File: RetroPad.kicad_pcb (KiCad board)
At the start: 2 copper layers, 125 x 45 mm, 16 parts, among them J1 5747840-3

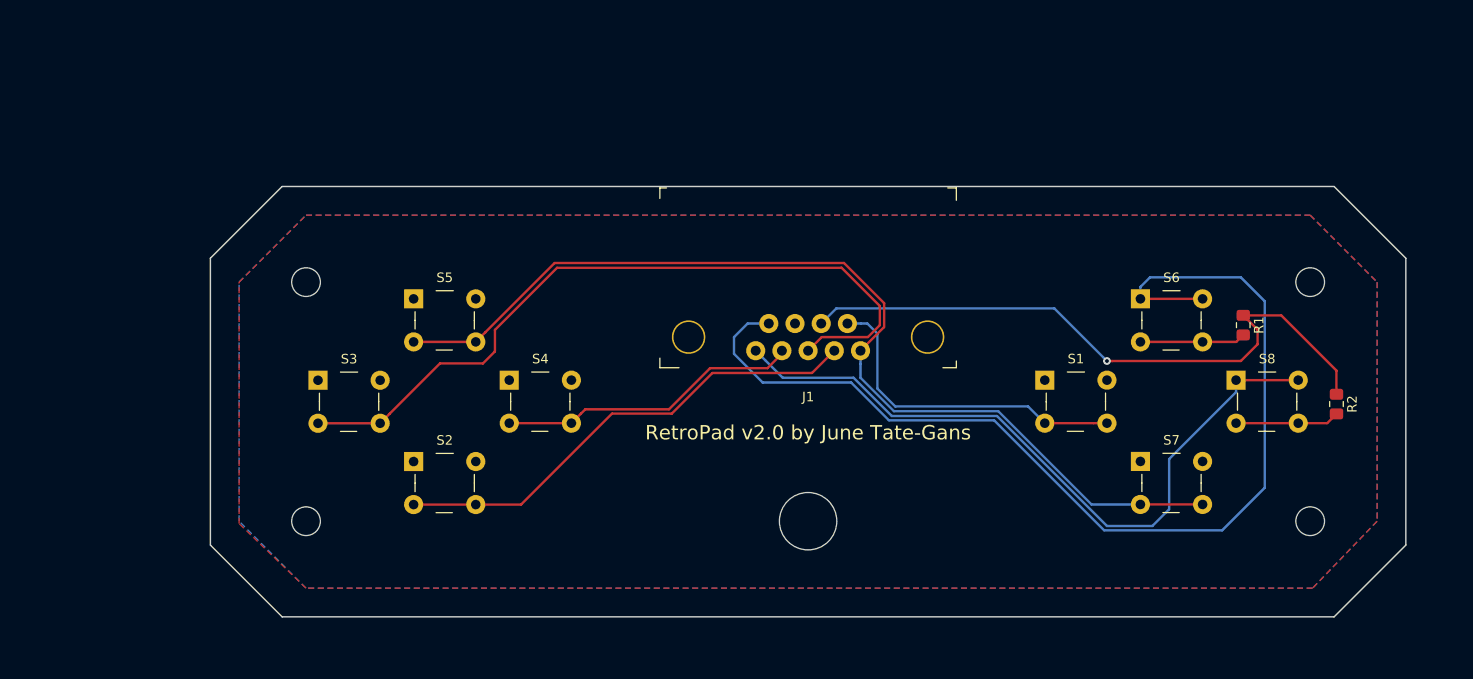
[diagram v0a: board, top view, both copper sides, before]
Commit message: Import of the new RetroPad v3.
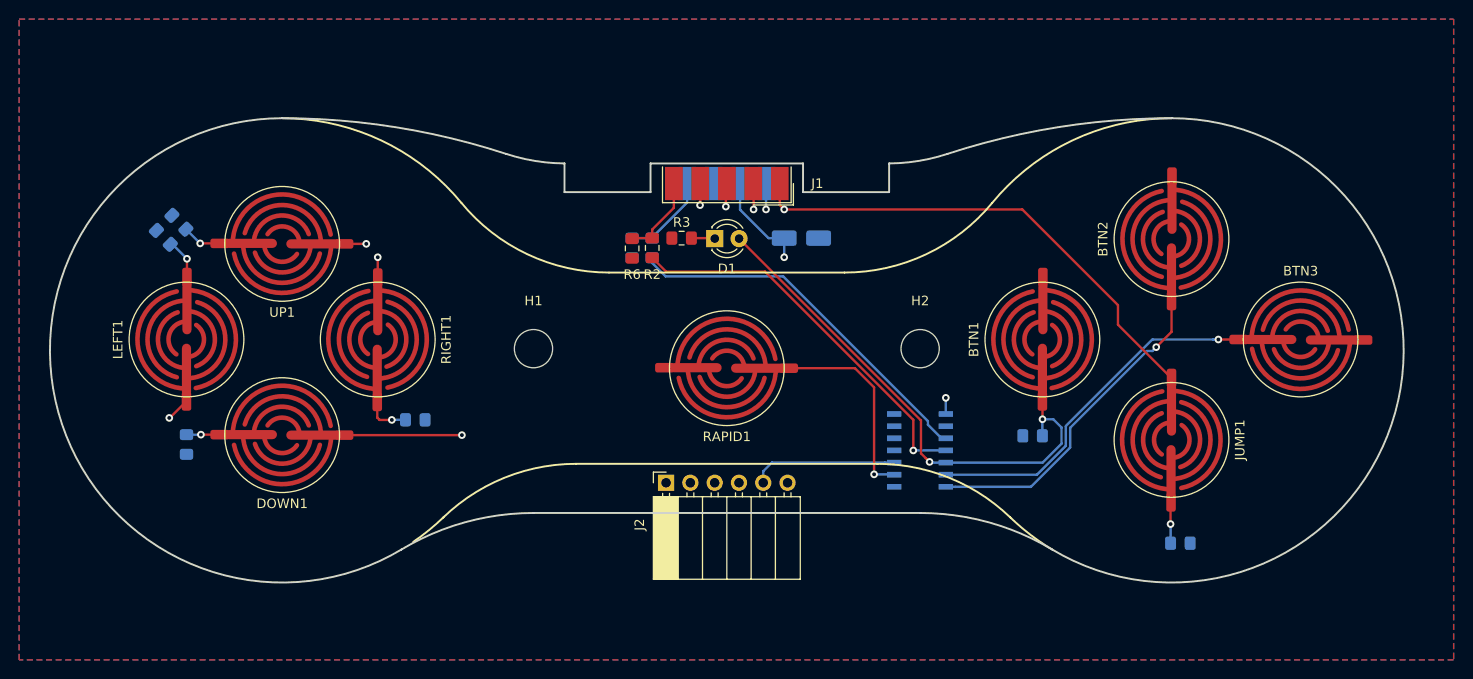
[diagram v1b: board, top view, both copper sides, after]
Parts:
- removed 3mm_LL, 3mm_LR, 3mm_UL, 3mm_UR: MountingHole_3mm, MountingHole:MountingHole_3mm
- removed 6mm_C: MountingHole_6mm, MountingHole:MountingHole_6mm
- removed S1: FIRE, digikey-footprints:Switch_Tactile_THT_B3F-1xxx
- removed S2: DOWN, digikey-footprints:Switch_Tactile_THT_B3F-1xxx
- removed S3: LEFT, digikey-footprints:Switch_Tactile_THT_B3F-1xxx
- removed S4: RIGHT, digikey-footprints:Switch_Tactile_THT_B3F-1xxx
- removed S5: UP, digikey-footprints:Switch_Tactile_THT_B3F-1xxx
- removed S6: FIRE2, digikey-footprints:Switch_Tactile_THT_B3F-1xxx
- removed S7: JUMP, digikey-footprints:Switch_Tactile_THT_B3F-1xxx
- removed S8: FIRE3, digikey-footprints:Switch_Tactile_THT_B3F-1xxx
- added BTN1: BTN1, RetroPad:Silicone_Membrane_Pad_11mm_(7.5mm), F.Cu at (183.0, 92.5)
- added BTN2: BTN2, RetroPad:Silicone_Membrane_Pad_11mm_(7.5mm), F.Cu at (196.5, 82.0)
- added BTN3: BTN3, RetroPad:Silicone_Membrane_Pad_11mm_(7.5mm), F.Cu at (210.0, 92.5)
- added C1: 0.1uF, Capacitor_SMD:CP_Elec_4x4.5, B.Cu at (157.8, 81.9)
- added D1: RAPID, LED_THT:LED_D3.0mm, F.Cu at (148.7, 82.0)
- added DOWN1: DOWN, RetroPad:Silicone_Membrane_Pad_11mm_(7.5mm), F.Cu at (103.5, 102.5)
- added H1: MountingHole, MountingHole:MountingHole_4mm, F.Cu at (129.8, 93.5)
- added H2: MountingHole, MountingHole:MountingHole_4mm, F.Cu at (170.2, 93.5)
- added J2: UPDI, Connector_PinSocket_2.54mm:PinSocket_1x06_P2.54mm_Horizontal, F.Cu at (143.7, 107.5)
- added JUMP1: JUMP, RetroPad:Silicone_Membrane_Pad_11mm_(7.5mm), F.Cu at (196.5, 103.0)
- added LEFT1: LEFT, RetroPad:Silicone_Membrane_Pad_11mm_(7.5mm), F.Cu at (93.5, 92.5)
- added R10: 0, Resistor_SMD:R_0805_2012Metric_Pad1.15x1.40mm_HandSolder, B.Cu at (91.1, 81.8)
- added R11: 0, Resistor_SMD:R_0805_2012Metric_Pad1.15x1.40mm_HandSolder, B.Cu at (117.4, 100.9)
- added R3: 330, Resistor_SMD:R_0805_2012Metric_Pad1.15x1.40mm_HandSolder, F.Cu at (145.3, 81.9)
- added R4: 1K, Resistor_SMD:R_0805_2012Metric_Pad1.15x1.40mm_HandSolder, B.Cu at (182.0, 102.6)
- added R5: 1K, Resistor_SMD:R_0805_2012Metric_Pad1.15x1.40mm_HandSolder, B.Cu at (140.1, 82.9)
- added R6: 1K, Resistor_SMD:R_0805_2012Metric_Pad1.15x1.40mm_HandSolder, F.Cu at (140.1, 83.0)
- added R7: 0, Resistor_SMD:R_0805_2012Metric_Pad1.15x1.40mm_HandSolder, B.Cu at (197.4, 113.8)
- added R8: 0, Resistor_SMD:R_0805_2012Metric_Pad1.15x1.40mm_HandSolder, B.Cu at (92.7, 80.2)
- added R9: 0, Resistor_SMD:R_0805_2012Metric_Pad1.15x1.40mm_HandSolder, B.Cu at (93.5, 103.5)
- added RAPID1: RAPID, RetroPad:Silicone_Membrane_Pad_11mm_(7.5mm), F.Cu at (150.0, 95.5)
- added RIGHT1: RIGHT, RetroPad:Silicone_Membrane_Pad_11mm_(7.5mm), F.Cu at (113.5, 92.5)
- added U1: ATtiny814-SS, Package_SO:SOIC-14_3.9x8.7mm_P1.27mm, B.Cu at (170.2, 104.1)
- added UP1: UP, RetroPad:Silicone_Membrane_Pad_11mm_(7.5mm), F.Cu at (103.5, 82.5)
- J1: value 5747840-3 -> DB9_Male; footprint digikey-footprints:DSUB-9_Jack_5747840-3 -> Connector_Dsub:DSUB-9_Male_EdgeMount_P2.77mm
- R1: value 330 -> 1K; moved to B.Cu
- R2: value 330 -> 1K
- moved R2 73.4 mm to (142.2, 82.9)
- moved R1 62.3 mm to (142.2, 82.9)
- moved J1 18.2 mm to (150.0, 76.2), turned to 180 degrees
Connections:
- J1 pad 7: /5V -> +5V
- J1 pad 8: /GND -> GND
- R1 pad 1: /5V -> /POTX
- R1 pad 2: Net-(R1-Pad2) -> /OUT_BTN3
- R2 pad 1: /5V -> /POTY
- R2 pad 2: Net-(R2-Pad2) -> /OUT_BTN2
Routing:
- net /POTX: track 112.9 -> 9.32 mm
- net /5V: track 67.6 -> 0.00 mm, vias 1 -> 0
- net /POTY: track 74.4 -> 8.76 mm
- net +5V: track 0.00 -> 54.7 mm, vias 0 -> 2
- net /OUT_BTN2: track 0.00 -> 40.9 mm, vias 0 -> 1
- net /OUT_BTN3: track 0.00 -> 39.1 mm
- net /BTN3: track 0.00 -> 37.7 mm, vias 0 -> 1
- net /BTN2: track 0.00 -> 34.8 mm, vias 0 -> 1
- net /FIRE: track 34.8 -> 60.9 mm, vias 0 -> 3
- net /RAPID: track 0.00 -> 21.0 mm, vias 0 -> 1
- net /LEFT: track 79.1 -> 96.5 mm, vias 0 -> 2
- net /DOWN: track 50.7 -> 68.1 mm, vias 0 -> 2
- net /RESET: track 0.00 -> 15.3 mm
- net Net-(R1-Pad2): track 11.1 -> 0.00 mm
- net Net-(R2-Pad2): track 10.9 -> 0.00 mm
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- added copper zone on B.Cu, net GND
- added copper zone on F.Cu, net GND
- added copper zone on In1.Cu, net GND
- added copper zone on In2.Cu, net GND
- removed copper zone on B.Cu, net /GND
- removed copper zone on F.Cu, net /GND
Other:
- board size 125 x 45 mm -> 141.6 x 48.6 mm
- copper layers 2 -> 4
- board text removed: "Open Source Hardware"
- board text removed: "RetroPad v2.0 by June Tate-Gans"
- board text removed: "http://github.com/jtgans/RetroPad"

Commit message: Fixed board outline.
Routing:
- net /OUT_BTN3: track 39.1 -> 39.7 mm
- net /DOWN: track 68.1 -> 67.4 mm
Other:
- outline, holes or cut-outs redrawn
